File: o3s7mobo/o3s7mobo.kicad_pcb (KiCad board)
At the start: 2 copper layers, 330 x 217 mm, 45 parts, among them M1541 M1541, M1543 M1543

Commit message: Per feedback, swapped keyboard DIN
Replaced 5-pin with 7-pin, so that while standard AT keyboards (and adapters) will still work, users can make PS/2 mouse adapters without needing an ATX form card or a case with a PS/2 mouse port
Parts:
- moved KEYBOARD 0.81 mm to (18.0, 26.5)
- renumbered REF** to AGP, REF** to ATXpower, REF** to ATpower, REF** to PS2, REF** to SATA1_0, REF** to SATA1_1, REF** to SATA1_2, REF** to SATA1_3, REF** to SDRAM1, REF** to SDRAM2, REF** to SDRAM3, REF** to SiI3114CTU, REF** to VT6212L

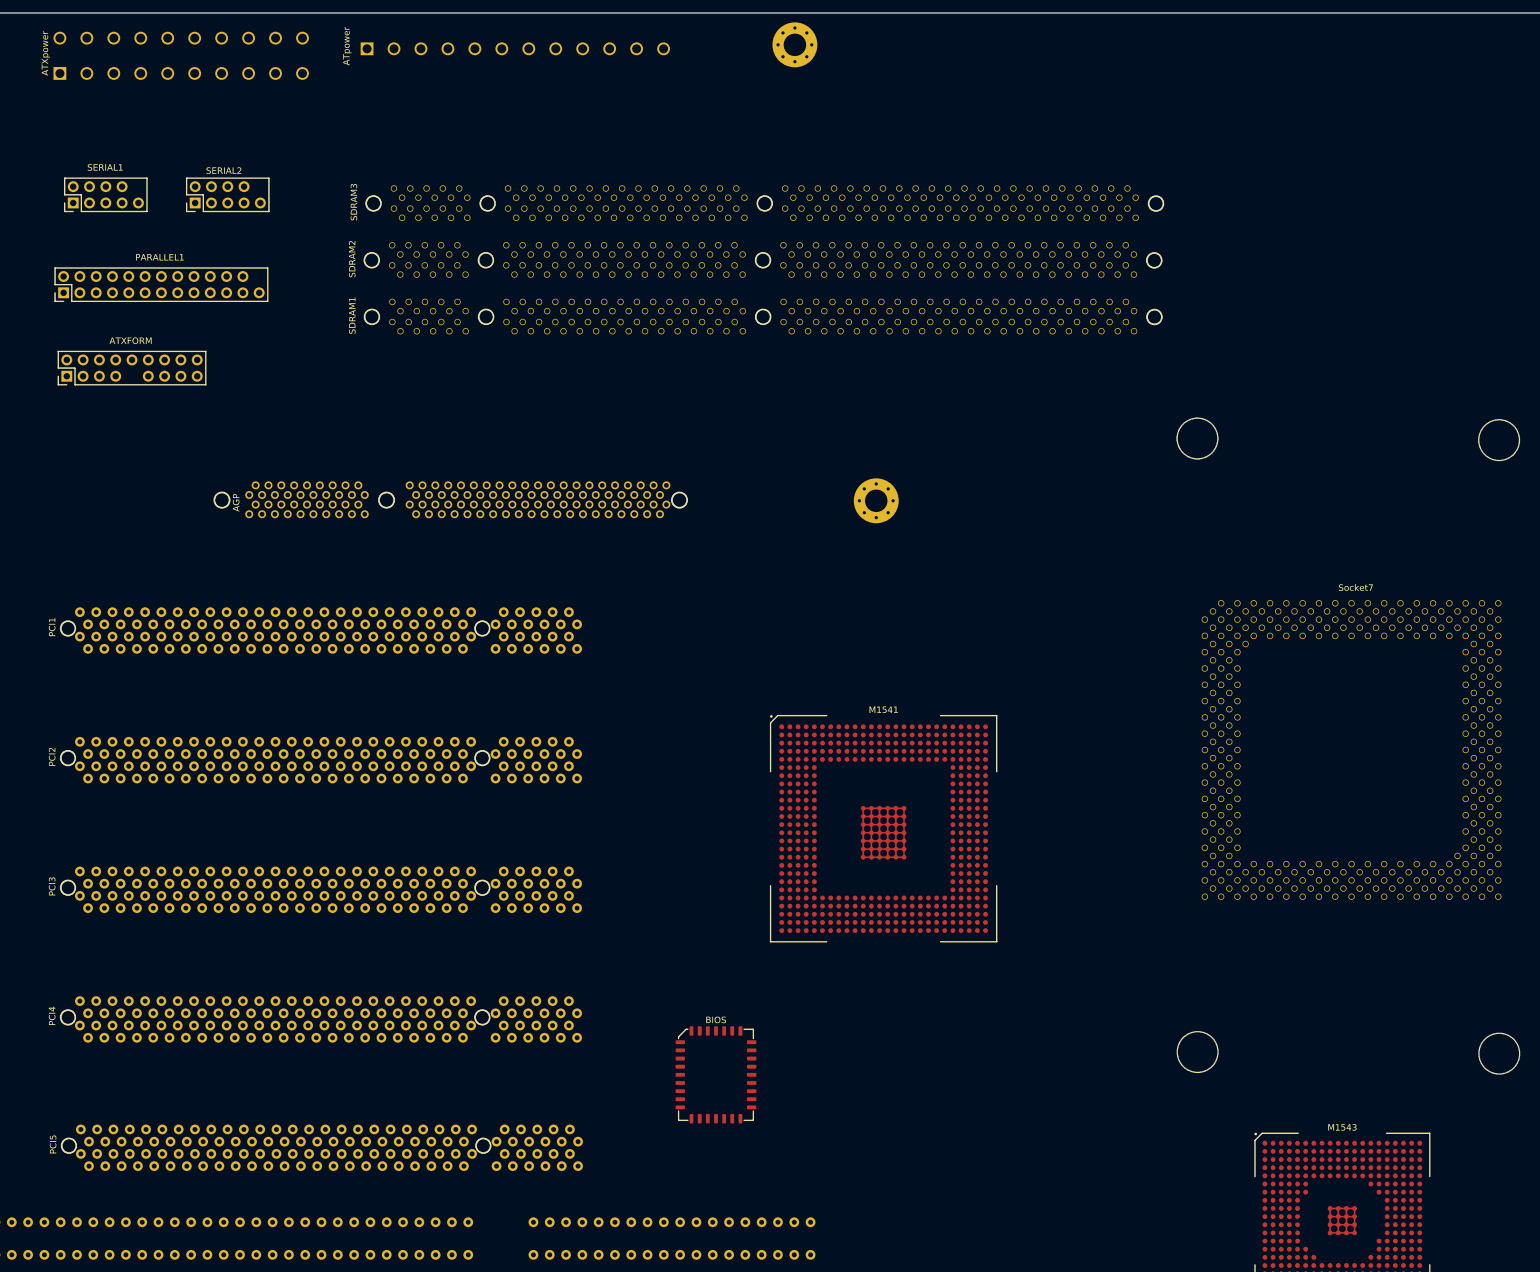
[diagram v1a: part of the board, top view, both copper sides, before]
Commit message: Added ATX and AT power schematics
This took way too long to figure out.
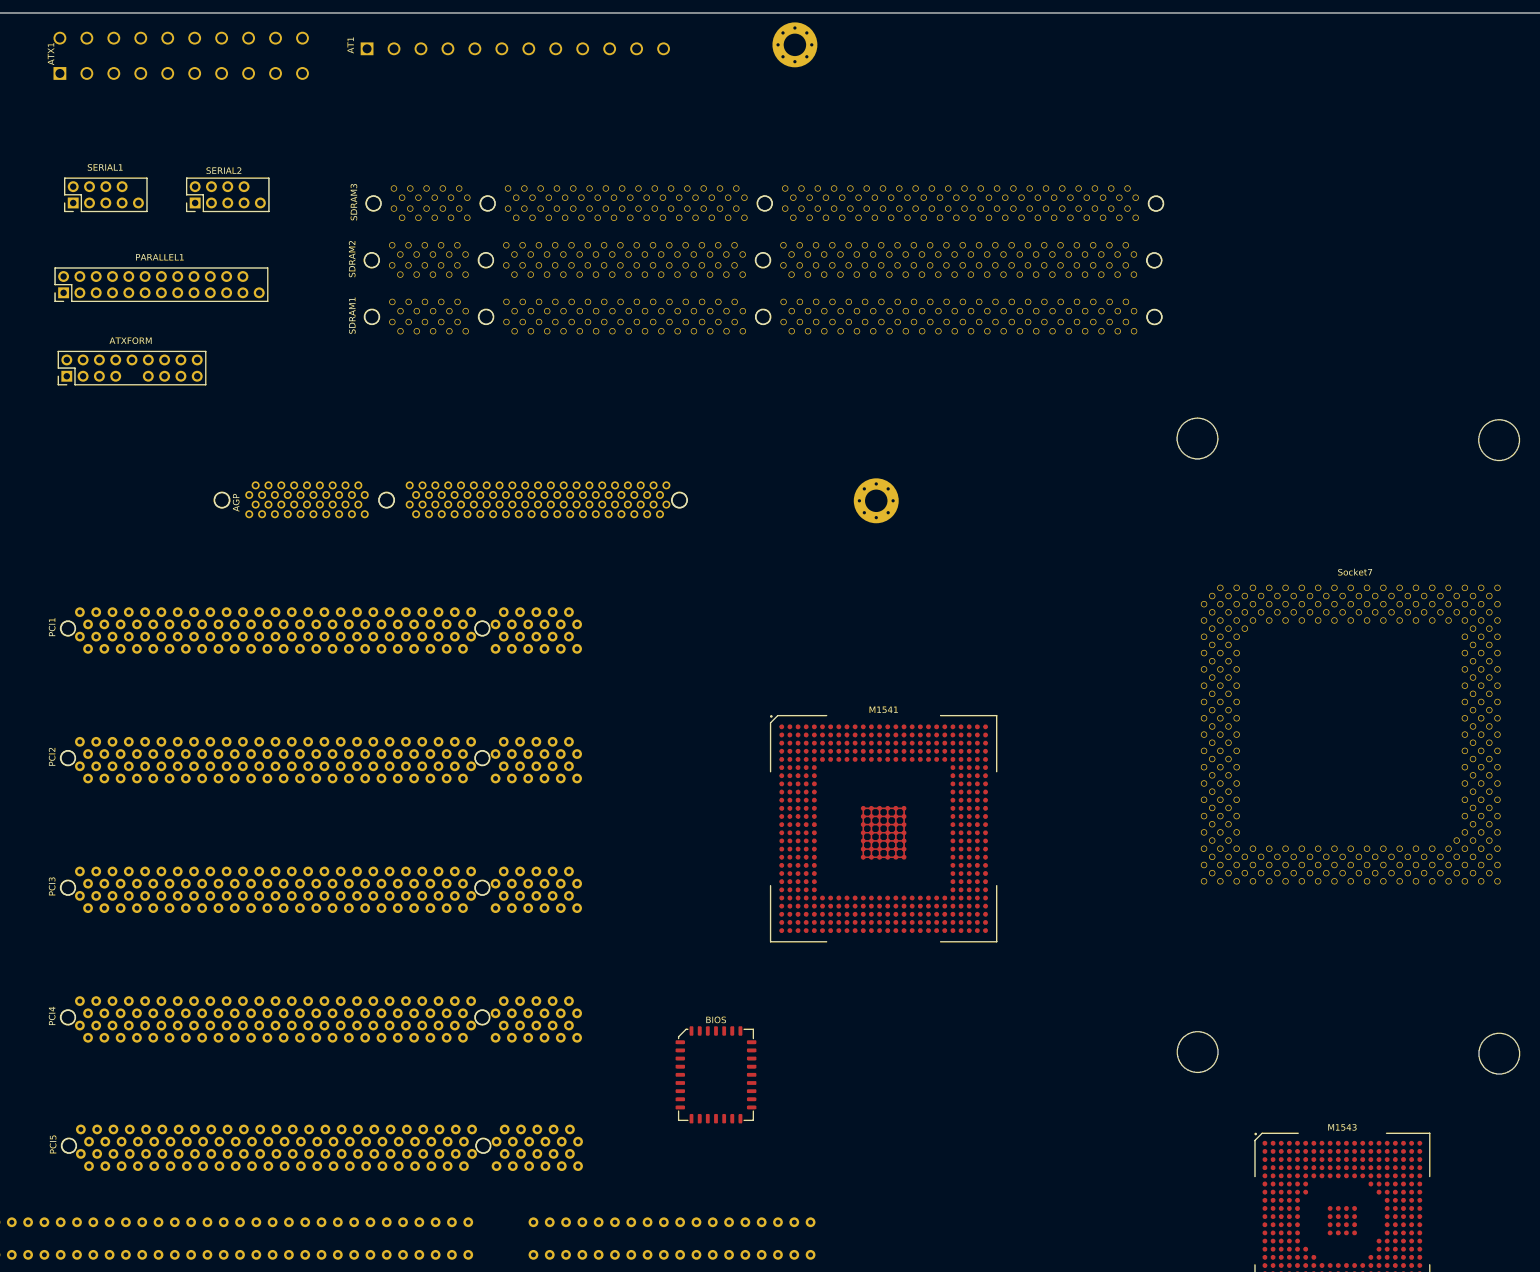
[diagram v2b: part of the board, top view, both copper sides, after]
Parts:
- removed ATXpower: ATXpower, Downloaded:ATXpower
- removed ATpower: ATpower, Downloaded:ATpower
- added AT1: AT-12, Downloaded:ATpower, F.Cu at (82.7, 4.00)
- added ATX1: ATX-20, Downloaded:ATXpower, F.Cu at (36.0, 5.35)
- moved Socket7 2.40 mm to (223.3, 86.8)
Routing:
- net (no net): track 120.6 -> 90.2 mm

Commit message: Added Socket 7 schematics
I'm willing to have these schematics uploaded to the official KiCAD repositories; I'm just unsure how.
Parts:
- removed Socket7: Socket_7, Downloaded:Socket_7
- added CPU1: Socket7, Downloaded:Socket_7, F.Cu at (223.3, 86.8)
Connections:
- net Net-(AT1-Pad1) renamed PWR_GOOD
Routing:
- net GND: track 0.00 -> 547.4 mm
- net Net-(CPU1-PadA19): track 0.00 -> 115.7 mm
- net Net-(CPU1-PadA11): track 0.00 -> 104.0 mm
- net PWR_+5V: track 0.00 -> 93.2 mm
- net PWR_-12V: track 0.00 -> 59.4 mm
- net PWR_-5V: track 0.00 -> 54.9 mm, vias 0 -> 1
- net PWR_+12V: track 0.00 -> 22.3 mm
- net PWR_+3.3V: track 0.00 -> 9.70 mm
- net Net-(CPU1-PadAN1): track 0.00 -> 2.54 mm
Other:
- copper layers 2 -> 4

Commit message: Been too long
Forgot I never pushed this.
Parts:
- removed M1541: M1541, Downloaded:M1541
- added NB1: M1542, Downloaded:M1541, F.Cu at (165.7, 117.3)
- PCI1, PCI2, PCI3, PCI4: value PCI -> Bus_PCI_32bit_5V
- moved CPU1 57.2 mm to (253.7, 135.3), turned to 180 degrees
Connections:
- CPU1 pad A31: /D22 -> CPU_D22
- CPU1 pad A33: /D18 -> CPU_D18
- CPU1 pad A35: /D15 -> CPU_D15
- CPU1 pad A5: /D41 -> CPU_D41
- CPU1 pad AE33: /A23 -> CPU_A23
- CPU1 pad AF34: /A21 -> CPU_A21
- CPU1 pad AG33: /A27 -> CPU_A27
- CPU1 pad AG35: /A24 -> CPU_A24
- CPU1 pad AH34: /A26 -> CPU_A26
- CPU1 pad AH36: /A22 -> CPU_A22
- CPU1 pad AJ33: /A31 -> CPU_A31
- CPU1 pad AJ35: /A25 -> CPU_A25
- CPU1 pad AK22: /A19 -> CPU_A19
- CPU1 pad AK24: /A17 -> CPU_A17
- CPU1 pad AK26: /A15 -> CPU_A15
- CPU1 pad AK28: /A13 -> CPU_A13
- CPU1 pad AK30: /A9 -> CPU_A9
- CPU1 pad AK32: /A5 -> CPU_A5
- CPU1 pad AK34: /A29 -> CPU_A29
- CPU1 pad AK36: /A28 -> CPU_A28
- CPU1 pad AL21: /A20 -> CPU_A20
- CPU1 pad AL23: /A18 -> CPU_A18
- CPU1 pad AL25: /A16 -> CPU_A16
- CPU1 pad AL27: /A14 -> CPU_A14
- CPU1 pad AL29: /A12 -> CPU_A12
- CPU1 pad AL31: /A11 -> CPU_A11
- CPU1 pad AL33: /A7 -> CPU_A7
- CPU1 pad AL35: /A3 -> CPU_A3
- CPU1 pad AM32: /A8 -> CPU_A8
- CPU1 pad AM34: /A4 -> CPU_A4
- CPU1 pad AM36: /A30 -> CPU_A30
- CPU1 pad AN31: /A10 -> CPU_A10
- CPU1 pad AN33: /A6 -> CPU_A6
- CPU1 pad B30: /D20 -> CPU_D20
- CPU1 pad B32: /D16 -> CPU_D16
- CPU1 pad B34: /D13 -> CPU_D13
- CPU1 pad B36: /D11 -> CPU_D11
- CPU1 pad B4: /D43 -> CPU_D43
- CPU1 pad C11: /D36 -> CPU_D36
- CPU1 pad C13: /D34 -> CPU_D34
- CPU1 pad C15: /D32 -> CPU_D32
- CPU1 pad C17: /D31 -> CPU_D31
- CPU1 pad C19: /D29 -> CPU_D29
- CPU1 pad C21: /D27 -> CPU_D27
- CPU1 pad C23: /D25 -> CPU_D25
- CPU1 pad C27: /D24 -> CPU_D24
- CPU1 pad C29: /D21 -> CPU_D21
- CPU1 pad C3: /D47 -> CPU_D47
- CPU1 pad C31: /D17 -> CPU_D17
- CPU1 pad C33: /D14 -> CPU_D14
- CPU1 pad C35: /D10 -> CPU_D10
- CPU1 pad C37: /D9 -> CPU_D9
- CPU1 pad C5: /D45 -> CPU_D45
- CPU1 pad C9: /D38 -> CPU_D38
- CPU1 pad D10: /D39 -> CPU_D39
- CPU1 pad D12: /D37 -> CPU_D37
- CPU1 pad D14: /D35 -> CPU_D35
- CPU1 pad D16: /D33 -> CPU_D33
- CPU1 pad D2: /D50 -> CPU_D50
- CPU1 pad D20: /D30 -> CPU_D30
- CPU1 pad D22: /D28 -> CPU_D28
- CPU1 pad D24: /D26 -> CPU_D26
- CPU1 pad D26: /D23 -> CPU_D23
- CPU1 pad D28: /D19 -> CPU_D19
- CPU1 pad D32: /D12 -> CPU_D12
- CPU1 pad D34: /D8 -> CPU_D8
- CPU1 pad D4: /D48 -> CPU_D48
- CPU1 pad D6: /D44 -> CPU_D44
- CPU1 pad D8: /D40 -> CPU_D40
- CPU1 pad E1: /D54 -> CPU_D54
- CPU1 pad E3: /D52 -> CPU_D52
- CPU1 pad E33: /D7 -> CPU_D7
- CPU1 pad E35: /D6 -> CPU_D6
- CPU1 pad E5: /D49 -> CPU_D49
- CPU1 pad E7: /D46 -> CPU_D46
- CPU1 pad E9: /D42 -> CPU_D42
- CPU1 pad F34: /D5 -> CPU_D5
- CPU1 pad F36: /D4 -> CPU_D4
- CPU1 pad F4: /D51 -> CPU_D51
- CPU1 pad G3: /D55 -> CPU_D55
- CPU1 pad G33: /D3 -> CPU_D3
- CPU1 pad G35: /D1 -> CPU_D1
- CPU1 pad G5: /D53 -> CPU_D53
- CPU1 pad H4: /D56 -> CPU_D56
- CPU1 pad J3: /D57 -> CPU_D57
- CPU1 pad J35: /D2 -> CPU_D2
- CPU1 pad J5: /D58 -> CPU_D58
- CPU1 pad K34: /D0 -> CPU_D0
- CPU1 pad K4: /D59 -> CPU_D59
- CPU1 pad L3: /D61 -> CPU_D61
- CPU1 pad L5: /D60 -> CPU_D60
- CPU1 pad M4: /D62 -> CPU_D62
- CPU1 pad N3: /D63 -> CPU_D63
- PCI1 pad A1: (no net) -> Net-(PCI1-PadA1)
- PCI1 pad A10: (no net) -> Net-(PCI1-PadA10)
- PCI1 pad A11: (no net) -> Net-(PCI1-PadA11)
- PCI1 pad A12: (no net) -> Net-(PCI1-PadA12)
- PCI1 pad A13: (no net) -> Net-(PCI1-PadA13)
- PCI1 pad A14: (no net) -> Net-(PCI1-PadA14)
- PCI1 pad A15: (no net) -> Net-(PCI1-PadA15)
- PCI1 pad A16: (no net) -> Net-(PCI1-PadA16)
- PCI1 pad A17: (no net) -> Net-(PCI1-PadA17)
- PCI1 pad A18: (no net) -> Net-(PCI1-PadA18)
- PCI1 pad A19: (no net) -> Net-(PCI1-PadA19)
- PCI1 pad A2: (no net) -> Net-(PCI1-PadA2)
- PCI1 pad A20: (no net) -> Net-(PCI1-PadA20)
- PCI1 pad A21: (no net) -> Net-(PCI1-PadA21)
- PCI1 pad A22: (no net) -> Net-(PCI1-PadA22)
- PCI1 pad A23: (no net) -> Net-(PCI1-PadA23)
- PCI1 pad A24: (no net) -> Net-(PCI1-PadA24)
- PCI1 pad A25: (no net) -> Net-(PCI1-PadA25)
- PCI1 pad A26: (no net) -> Net-(PCI1-PadA26)
- PCI1 pad A27: (no net) -> Net-(PCI1-PadA27)
- PCI1 pad A28: (no net) -> Net-(PCI1-PadA28)
- PCI1 pad A29: (no net) -> Net-(PCI1-PadA29)
- PCI1 pad A3: (no net) -> Net-(PCI1-PadA3)
- PCI1 pad A30: (no net) -> Net-(PCI1-PadA30)
- PCI1 pad A31: (no net) -> Net-(PCI1-PadA31)
- PCI1 pad A32: (no net) -> Net-(PCI1-PadA32)
- PCI1 pad A33: (no net) -> Net-(PCI1-PadA33)
- PCI1 pad A34: (no net) -> Net-(PCI1-PadA34)
- PCI1 pad A35: (no net) -> Net-(PCI1-PadA35)
- PCI1 pad A36: (no net) -> Net-(PCI1-PadA36)
- PCI1 pad A37: (no net) -> Net-(PCI1-PadA37)
- PCI1 pad A38: (no net) -> Net-(PCI1-PadA38)
- PCI1 pad A39: (no net) -> Net-(PCI1-PadA39)
- PCI1 pad A4: (no net) -> Net-(PCI1-PadA4)
- PCI1 pad A40: (no net) -> Net-(PCI1-PadA40)
- PCI1 pad A41: (no net) -> Net-(PCI1-PadA41)
- PCI1 pad A42: (no net) -> Net-(PCI1-PadA42)
- PCI1 pad A43: (no net) -> Net-(PCI1-PadA43)
- PCI1 pad A44: (no net) -> Net-(PCI1-PadA44)
- PCI1 pad A45: (no net) -> Net-(PCI1-PadA45)
- PCI1 pad A46: (no net) -> Net-(PCI1-PadA46)
- PCI1 pad A47: (no net) -> Net-(PCI1-PadA47)
- PCI1 pad A48: (no net) -> Net-(PCI1-PadA48)
- PCI1 pad A49: (no net) -> Net-(PCI1-PadA49)
- PCI1 pad A5: (no net) -> Net-(PCI1-PadA5)
- PCI1 pad A52: (no net) -> Net-(PCI1-PadA52)
- PCI1 pad A53: (no net) -> Net-(PCI1-PadA53)
- PCI1 pad A54: (no net) -> Net-(PCI1-PadA54)
- PCI1 pad A55: (no net) -> Net-(PCI1-PadA55)
- PCI1 pad A56: (no net) -> Net-(PCI1-PadA56)
- PCI1 pad A57: (no net) -> Net-(PCI1-PadA57)
- PCI1 pad A58: (no net) -> Net-(PCI1-PadA58)
- PCI1 pad A59: (no net) -> Net-(PCI1-PadA59)
- PCI1 pad A6: (no net) -> Net-(PCI1-PadA6)
- PCI1 pad A60: (no net) -> Net-(PCI1-PadA60)
- PCI1 pad A61: (no net) -> Net-(PCI1-PadA61)
- PCI1 pad A62: (no net) -> Net-(PCI1-PadA62)
- PCI1 pad A7: (no net) -> Net-(PCI1-PadA7)
- PCI1 pad A8: (no net) -> Net-(PCI1-PadA8)
- PCI1 pad A9: (no net) -> Net-(PCI1-PadA9)
- PCI1 pad B1: (no net) -> Net-(PCI1-PadB1)
- PCI1 pad B10: (no net) -> Net-(PCI1-PadB10)
- PCI1 pad B11: (no net) -> Net-(PCI1-PadB11)
- PCI1 pad B12: (no net) -> Net-(PCI1-PadB12)
- PCI1 pad B13: (no net) -> Net-(PCI1-PadB13)
- PCI1 pad B14: (no net) -> Net-(PCI1-PadB14)
- PCI1 pad B15: (no net) -> Net-(PCI1-PadB15)
- PCI1 pad B16: (no net) -> Net-(PCI1-PadB16)
- PCI1 pad B17: (no net) -> Net-(PCI1-PadB17)
- PCI1 pad B18: (no net) -> Net-(PCI1-PadB18)
- PCI1 pad B19: (no net) -> Net-(PCI1-PadB19)
- PCI1 pad B2: (no net) -> Net-(PCI1-PadB2)
- PCI1 pad B20: (no net) -> Net-(PCI1-PadB20)
- PCI1 pad B21: (no net) -> Net-(PCI1-PadB21)
- PCI1 pad B22: (no net) -> Net-(PCI1-PadB22)
- PCI1 pad B23: (no net) -> Net-(PCI1-PadB23)
- PCI1 pad B24: (no net) -> Net-(PCI1-PadB24)
- PCI1 pad B25: (no net) -> Net-(PCI1-PadB25)
- PCI1 pad B26: (no net) -> Net-(PCI1-PadB26)
- PCI1 pad B27: (no net) -> Net-(PCI1-PadB27)
- PCI1 pad B28: (no net) -> Net-(PCI1-PadB28)
- PCI1 pad B29: (no net) -> Net-(PCI1-PadB29)
- PCI1 pad B3: (no net) -> Net-(PCI1-PadB3)
- PCI1 pad B30: (no net) -> Net-(PCI1-PadB30)
- PCI1 pad B31: (no net) -> Net-(PCI1-PadB31)
- PCI1 pad B32: (no net) -> Net-(PCI1-PadB32)
- PCI1 pad B33: (no net) -> Net-(PCI1-PadB33)
- PCI1 pad B34: (no net) -> Net-(PCI1-PadB34)
- PCI1 pad B35: (no net) -> Net-(PCI1-PadB35)
- PCI1 pad B36: (no net) -> Net-(PCI1-PadB36)
- PCI1 pad B37: (no net) -> Net-(PCI1-PadB37)
- PCI1 pad B38: (no net) -> Net-(PCI1-PadB38)
- PCI1 pad B39: (no net) -> Net-(PCI1-PadB39)
- PCI1 pad B4: (no net) -> Net-(PCI1-PadB4)
- PCI1 pad B40: (no net) -> Net-(PCI1-PadB40)
- PCI1 pad B41: (no net) -> Net-(PCI1-PadB41)
- PCI1 pad B42: (no net) -> Net-(PCI1-PadB42)
- PCI1 pad B43: (no net) -> Net-(PCI1-PadB43)
- PCI1 pad B44: (no net) -> Net-(PCI1-PadB44)
- PCI1 pad B45: (no net) -> Net-(PCI1-PadB45)
- PCI1 pad B46: (no net) -> Net-(PCI1-PadB46)
- PCI1 pad B47: (no net) -> Net-(PCI1-PadB47)
- PCI1 pad B48: (no net) -> Net-(PCI1-PadB48)
- PCI1 pad B49: (no net) -> Net-(PCI1-PadB49)
- PCI1 pad B5: (no net) -> Net-(PCI1-PadB5)
- PCI1 pad B52: (no net) -> Net-(PCI1-PadB52)
- PCI1 pad B53: (no net) -> Net-(PCI1-PadB53)
- PCI1 pad B54: (no net) -> Net-(PCI1-PadB54)
- PCI1 pad B55: (no net) -> Net-(PCI1-PadB55)
- PCI1 pad B56: (no net) -> Net-(PCI1-PadB56)
- PCI1 pad B57: (no net) -> Net-(PCI1-PadB57)
- PCI1 pad B58: (no net) -> Net-(PCI1-PadB58)
- PCI1 pad B59: (no net) -> Net-(PCI1-PadB59)
- PCI1 pad B6: (no net) -> Net-(PCI1-PadB6)
- PCI1 pad B60: (no net) -> Net-(PCI1-PadB60)
- PCI1 pad B61: (no net) -> Net-(PCI1-PadB61)
- PCI1 pad B62: (no net) -> Net-(PCI1-PadB62)
- PCI1 pad B7: (no net) -> Net-(PCI1-PadB7)
- PCI1 pad B8: (no net) -> Net-(PCI1-PadB8)
- PCI1 pad B9: (no net) -> Net-(PCI1-PadB9)
- PCI2 pad A1: (no net) -> Net-(PCI2-PadA1)
- PCI2 pad A10: (no net) -> Net-(PCI2-PadA10)
- PCI2 pad A11: (no net) -> Net-(PCI2-PadA11)
- PCI2 pad A12: (no net) -> Net-(PCI2-PadA12)
- PCI2 pad A13: (no net) -> Net-(PCI2-PadA13)
- PCI2 pad A14: (no net) -> Net-(PCI2-PadA14)
- PCI2 pad A15: (no net) -> Net-(PCI2-PadA15)
- PCI2 pad A16: (no net) -> Net-(PCI2-PadA16)
- PCI2 pad A17: (no net) -> Net-(PCI2-PadA17)
- PCI2 pad A18: (no net) -> Net-(PCI2-PadA18)
- PCI2 pad A19: (no net) -> Net-(PCI2-PadA19)
- PCI2 pad A2: (no net) -> Net-(PCI2-PadA2)
- PCI2 pad A20: (no net) -> Net-(PCI2-PadA20)
- PCI2 pad A21: (no net) -> Net-(PCI2-PadA21)
- PCI2 pad A22: (no net) -> Net-(PCI2-PadA22)
- PCI2 pad A23: (no net) -> Net-(PCI2-PadA23)
- PCI2 pad A24: (no net) -> Net-(PCI2-PadA24)
- PCI2 pad A25: (no net) -> Net-(PCI2-PadA25)
- PCI2 pad A26: (no net) -> Net-(PCI2-PadA26)
- PCI2 pad A27: (no net) -> Net-(PCI2-PadA27)
- PCI2 pad A28: (no net) -> Net-(PCI2-PadA28)
- PCI2 pad A29: (no net) -> Net-(PCI2-PadA29)
- PCI2 pad A3: (no net) -> Net-(PCI2-PadA3)
- PCI2 pad A30: (no net) -> Net-(PCI2-PadA30)
- PCI2 pad A31: (no net) -> Net-(PCI2-PadA31)
- PCI2 pad A32: (no net) -> Net-(PCI2-PadA32)
- PCI2 pad A33: (no net) -> Net-(PCI2-PadA33)
- PCI2 pad A34: (no net) -> Net-(PCI2-PadA34)
- PCI2 pad A35: (no net) -> Net-(PCI2-PadA35)
- PCI2 pad A36: (no net) -> Net-(PCI2-PadA36)
- PCI2 pad A37: (no net) -> Net-(PCI2-PadA37)
- PCI2 pad A38: (no net) -> Net-(PCI2-PadA38)
- PCI2 pad A39: (no net) -> Net-(PCI2-PadA39)
- PCI2 pad A4: (no net) -> Net-(PCI2-PadA4)
- PCI2 pad A40: (no net) -> Net-(PCI2-PadA40)
- PCI2 pad A41: (no net) -> Net-(PCI2-PadA41)
- PCI2 pad A42: (no net) -> Net-(PCI2-PadA42)
- PCI2 pad A43: (no net) -> Net-(PCI2-PadA43)
- PCI2 pad A44: (no net) -> Net-(PCI2-PadA44)
- PCI2 pad A45: (no net) -> Net-(PCI2-PadA45)
- PCI2 pad A46: (no net) -> Net-(PCI2-PadA46)
- PCI2 pad A47: (no net) -> Net-(PCI2-PadA47)
- PCI2 pad A48: (no net) -> Net-(PCI2-PadA48)
- PCI2 pad A49: (no net) -> Net-(PCI2-PadA49)
- PCI2 pad A5: (no net) -> Net-(PCI2-PadA5)
- PCI2 pad A52: (no net) -> Net-(PCI2-PadA52)
- PCI2 pad A53: (no net) -> Net-(PCI2-PadA53)
- PCI2 pad A54: (no net) -> Net-(PCI2-PadA54)
- PCI2 pad A55: (no net) -> Net-(PCI2-PadA55)
- PCI2 pad A56: (no net) -> Net-(PCI2-PadA56)
- PCI2 pad A57: (no net) -> Net-(PCI2-PadA57)
- PCI2 pad A58: (no net) -> Net-(PCI2-PadA58)
- PCI2 pad A59: (no net) -> Net-(PCI2-PadA59)
- PCI2 pad A6: (no net) -> Net-(PCI2-PadA6)
- PCI2 pad A60: (no net) -> Net-(PCI2-PadA60)
- PCI2 pad A61: (no net) -> Net-(PCI2-PadA61)
- PCI2 pad A62: (no net) -> Net-(PCI2-PadA62)
- PCI2 pad A7: (no net) -> Net-(PCI2-PadA7)
- PCI2 pad A8: (no net) -> Net-(PCI2-PadA8)
- PCI2 pad A9: (no net) -> Net-(PCI2-PadA9)
- PCI2 pad B1: (no net) -> Net-(PCI2-PadB1)
- PCI2 pad B10: (no net) -> Net-(PCI2-PadB10)
- PCI2 pad B11: (no net) -> Net-(PCI2-PadB11)
- PCI2 pad B12: (no net) -> Net-(PCI2-PadB12)
- PCI2 pad B13: (no net) -> Net-(PCI2-PadB13)
- PCI2 pad B14: (no net) -> Net-(PCI2-PadB14)
- PCI2 pad B15: (no net) -> Net-(PCI2-PadB15)
- PCI2 pad B16: (no net) -> Net-(PCI2-PadB16)
- PCI2 pad B17: (no net) -> Net-(PCI2-PadB17)
- PCI2 pad B18: (no net) -> Net-(PCI2-PadB18)
- PCI2 pad B19: (no net) -> Net-(PCI2-PadB19)
- PCI2 pad B2: (no net) -> Net-(PCI2-PadB2)
- PCI2 pad B20: (no net) -> Net-(PCI2-PadB20)
- PCI2 pad B21: (no net) -> Net-(PCI2-PadB21)
- PCI2 pad B22: (no net) -> Net-(PCI2-PadB22)
- PCI2 pad B23: (no net) -> Net-(PCI2-PadB23)
- PCI2 pad B24: (no net) -> Net-(PCI2-PadB24)
- PCI2 pad B25: (no net) -> Net-(PCI2-PadB25)
- PCI2 pad B26: (no net) -> Net-(PCI2-PadB26)
- PCI2 pad B27: (no net) -> Net-(PCI2-PadB27)
- PCI2 pad B28: (no net) -> Net-(PCI2-PadB28)
- PCI2 pad B29: (no net) -> Net-(PCI2-PadB29)
- PCI2 pad B3: (no net) -> Net-(PCI2-PadB3)
- PCI2 pad B30: (no net) -> Net-(PCI2-PadB30)
- PCI2 pad B31: (no net) -> Net-(PCI2-PadB31)
- PCI2 pad B32: (no net) -> Net-(PCI2-PadB32)
- PCI2 pad B33: (no net) -> Net-(PCI2-PadB33)
- PCI2 pad B34: (no net) -> Net-(PCI2-PadB34)
- PCI2 pad B35: (no net) -> Net-(PCI2-PadB35)
- PCI2 pad B36: (no net) -> Net-(PCI2-PadB36)
- PCI2 pad B37: (no net) -> Net-(PCI2-PadB37)
- PCI2 pad B38: (no net) -> Net-(PCI2-PadB38)
- PCI2 pad B39: (no net) -> Net-(PCI2-PadB39)
- PCI2 pad B4: (no net) -> Net-(PCI2-PadB4)
- PCI2 pad B40: (no net) -> Net-(PCI2-PadB40)
- PCI2 pad B41: (no net) -> Net-(PCI2-PadB41)
- PCI2 pad B42: (no net) -> Net-(PCI2-PadB42)
- PCI2 pad B43: (no net) -> Net-(PCI2-PadB43)
- PCI2 pad B44: (no net) -> Net-(PCI2-PadB44)
- PCI2 pad B45: (no net) -> Net-(PCI2-PadB45)
- PCI2 pad B46: (no net) -> Net-(PCI2-PadB46)
- PCI2 pad B47: (no net) -> Net-(PCI2-PadB47)
- PCI2 pad B48: (no net) -> Net-(PCI2-PadB48)
- PCI2 pad B49: (no net) -> Net-(PCI2-PadB49)
- PCI2 pad B5: (no net) -> Net-(PCI2-PadB5)
- PCI2 pad B52: (no net) -> Net-(PCI2-PadB52)
- PCI2 pad B53: (no net) -> Net-(PCI2-PadB53)
- PCI2 pad B54: (no net) -> Net-(PCI2-PadB54)
- PCI2 pad B55: (no net) -> Net-(PCI2-PadB55)
- PCI2 pad B56: (no net) -> Net-(PCI2-PadB56)
- PCI2 pad B57: (no net) -> Net-(PCI2-PadB57)
- PCI2 pad B58: (no net) -> Net-(PCI2-PadB58)
- PCI2 pad B59: (no net) -> Net-(PCI2-PadB59)
- PCI2 pad B6: (no net) -> Net-(PCI2-PadB6)
- PCI2 pad B60: (no net) -> Net-(PCI2-PadB60)
- PCI2 pad B61: (no net) -> Net-(PCI2-PadB61)
- PCI2 pad B62: (no net) -> Net-(PCI2-PadB62)
- PCI2 pad B7: (no net) -> Net-(PCI2-PadB7)
- PCI2 pad B8: (no net) -> Net-(PCI2-PadB8)
- PCI2 pad B9: (no net) -> Net-(PCI2-PadB9)
- PCI3 pad A1: (no net) -> Net-(PCI3-PadA1)
- PCI3 pad A10: (no net) -> Net-(PCI3-PadA10)
- PCI3 pad A11: (no net) -> Net-(PCI3-PadA11)
- PCI3 pad A12: (no net) -> Net-(PCI3-PadA12)
- PCI3 pad A13: (no net) -> Net-(PCI3-PadA13)
- PCI3 pad A14: (no net) -> Net-(PCI3-PadA14)
- PCI3 pad A15: (no net) -> Net-(PCI3-PadA15)
- PCI3 pad A16: (no net) -> Net-(PCI3-PadA16)
- PCI3 pad A17: (no net) -> Net-(PCI3-PadA17)
- PCI3 pad A18: (no net) -> Net-(PCI3-PadA18)
- PCI3 pad A19: (no net) -> Net-(PCI3-PadA19)
- PCI3 pad A2: (no net) -> Net-(PCI3-PadA2)
- PCI3 pad A20: (no net) -> Net-(PCI3-PadA20)
- PCI3 pad A21: (no net) -> Net-(PCI3-PadA21)
- PCI3 pad A22: (no net) -> Net-(PCI3-PadA22)
- PCI3 pad A23: (no net) -> Net-(PCI3-PadA23)
- PCI3 pad A24: (no net) -> Net-(PCI3-PadA24)
- PCI3 pad A25: (no net) -> Net-(PCI3-PadA25)
- PCI3 pad A26: (no net) -> Net-(PCI3-PadA26)
- PCI3 pad A27: (no net) -> Net-(PCI3-PadA27)
- PCI3 pad A28: (no net) -> Net-(PCI3-PadA28)
- PCI3 pad A29: (no net) -> Net-(PCI3-PadA29)
- PCI3 pad A3: (no net) -> Net-(PCI3-PadA3)
- PCI3 pad A30: (no net) -> Net-(PCI3-PadA30)
- PCI3 pad A31: (no net) -> Net-(PCI3-PadA31)
- PCI3 pad A32: (no net) -> Net-(PCI3-PadA32)
- PCI3 pad A33: (no net) -> Net-(PCI3-PadA33)
- PCI3 pad A34: (no net) -> Net-(PCI3-PadA34)
- PCI3 pad A35: (no net) -> Net-(PCI3-PadA35)
- PCI3 pad A36: (no net) -> Net-(PCI3-PadA36)
- PCI3 pad A37: (no net) -> Net-(PCI3-PadA37)
- PCI3 pad A38: (no net) -> Net-(PCI3-PadA38)
- PCI3 pad A39: (no net) -> Net-(PCI3-PadA39)
- PCI3 pad A4: (no net) -> Net-(PCI3-PadA4)
- PCI3 pad A40: (no net) -> Net-(PCI3-PadA40)
- PCI3 pad A41: (no net) -> Net-(PCI3-PadA41)
- PCI3 pad A42: (no net) -> Net-(PCI3-PadA42)
- PCI3 pad A43: (no net) -> Net-(PCI3-PadA43)
- PCI3 pad A44: (no net) -> Net-(PCI3-PadA44)
- PCI3 pad A45: (no net) -> Net-(PCI3-PadA45)
- PCI3 pad A46: (no net) -> Net-(PCI3-PadA46)
- PCI3 pad A47: (no net) -> Net-(PCI3-PadA47)
- PCI3 pad A48: (no net) -> Net-(PCI3-PadA48)
- PCI3 pad A49: (no net) -> Net-(PCI3-PadA49)
- PCI3 pad A5: (no net) -> Net-(PCI3-PadA5)
- PCI3 pad A52: (no net) -> Net-(PCI3-PadA52)
- PCI3 pad A53: (no net) -> Net-(PCI3-PadA53)
- PCI3 pad A54: (no net) -> Net-(PCI3-PadA54)
- PCI3 pad A55: (no net) -> Net-(PCI3-PadA55)
- PCI3 pad A56: (no net) -> Net-(PCI3-PadA56)
- PCI3 pad A57: (no net) -> Net-(PCI3-PadA57)
- PCI3 pad A58: (no net) -> Net-(PCI3-PadA58)
- PCI3 pad A59: (no net) -> Net-(PCI3-PadA59)
- PCI3 pad A6: (no net) -> Net-(PCI3-PadA6)
- PCI3 pad A60: (no net) -> Net-(PCI3-PadA60)
- PCI3 pad A61: (no net) -> Net-(PCI3-PadA61)
- PCI3 pad A62: (no net) -> Net-(PCI3-PadA62)
- PCI3 pad A7: (no net) -> Net-(PCI3-PadA7)
- PCI3 pad A8: (no net) -> Net-(PCI3-PadA8)
- PCI3 pad A9: (no net) -> Net-(PCI3-PadA9)
- PCI3 pad B1: (no net) -> Net-(PCI3-PadB1)
- PCI3 pad B10: (no net) -> Net-(PCI3-PadB10)
- PCI3 pad B11: (no net) -> Net-(PCI3-PadB11)
- PCI3 pad B12: (no net) -> Net-(PCI3-PadB12)
- PCI3 pad B13: (no net) -> Net-(PCI3-PadB13)
- PCI3 pad B14: (no net) -> Net-(PCI3-PadB14)
- PCI3 pad B15: (no net) -> Net-(PCI3-PadB15)
- PCI3 pad B16: (no net) -> Net-(PCI3-PadB16)
- PCI3 pad B17: (no net) -> Net-(PCI3-PadB17)
- PCI3 pad B18: (no net) -> Net-(PCI3-PadB18)
- PCI3 pad B19: (no net) -> Net-(PCI3-PadB19)
- PCI3 pad B2: (no net) -> Net-(PCI3-PadB2)
- PCI3 pad B20: (no net) -> Net-(PCI3-PadB20)
- PCI3 pad B21: (no net) -> Net-(PCI3-PadB21)
- PCI3 pad B22: (no net) -> Net-(PCI3-PadB22)
- PCI3 pad B23: (no net) -> Net-(PCI3-PadB23)
- PCI3 pad B24: (no net) -> Net-(PCI3-PadB24)
- PCI3 pad B25: (no net) -> Net-(PCI3-PadB25)
- PCI3 pad B26: (no net) -> Net-(PCI3-PadB26)
- PCI3 pad B27: (no net) -> Net-(PCI3-PadB27)
- PCI3 pad B28: (no net) -> Net-(PCI3-PadB28)
- PCI3 pad B29: (no net) -> Net-(PCI3-PadB29)
- PCI3 pad B3: (no net) -> Net-(PCI3-PadB3)
- PCI3 pad B30: (no net) -> Net-(PCI3-PadB30)
- PCI3 pad B31: (no net) -> Net-(PCI3-PadB31)
- PCI3 pad B32: (no net) -> Net-(PCI3-PadB32)
- PCI3 pad B33: (no net) -> Net-(PCI3-PadB33)
- PCI3 pad B34: (no net) -> Net-(PCI3-PadB34)
- PCI3 pad B35: (no net) -> Net-(PCI3-PadB35)
- PCI3 pad B36: (no net) -> Net-(PCI3-PadB36)
- PCI3 pad B37: (no net) -> Net-(PCI3-PadB37)
- PCI3 pad B38: (no net) -> Net-(PCI3-PadB38)
- PCI3 pad B39: (no net) -> Net-(PCI3-PadB39)
- PCI3 pad B4: (no net) -> Net-(PCI3-PadB4)
- PCI3 pad B40: (no net) -> Net-(PCI3-PadB40)
- PCI3 pad B41: (no net) -> Net-(PCI3-PadB41)
- PCI3 pad B42: (no net) -> Net-(PCI3-PadB42)
- PCI3 pad B43: (no net) -> Net-(PCI3-PadB43)
- PCI3 pad B44: (no net) -> Net-(PCI3-PadB44)
- PCI3 pad B45: (no net) -> Net-(PCI3-PadB45)
- PCI3 pad B46: (no net) -> Net-(PCI3-PadB46)
- PCI3 pad B47: (no net) -> Net-(PCI3-PadB47)
- PCI3 pad B48: (no net) -> Net-(PCI3-PadB48)
- PCI3 pad B49: (no net) -> Net-(PCI3-PadB49)
- PCI3 pad B5: (no net) -> Net-(PCI3-PadB5)
- PCI3 pad B52: (no net) -> Net-(PCI3-PadB52)
- PCI3 pad B53: (no net) -> Net-(PCI3-PadB53)
- PCI3 pad B54: (no net) -> Net-(PCI3-PadB54)
- PCI3 pad B55: (no net) -> Net-(PCI3-PadB55)
- PCI3 pad B56: (no net) -> Net-(PCI3-PadB56)
- PCI3 pad B57: (no net) -> Net-(PCI3-PadB57)
- PCI3 pad B58: (no net) -> Net-(PCI3-PadB58)
- PCI3 pad B59: (no net) -> Net-(PCI3-PadB59)
- PCI3 pad B6: (no net) -> Net-(PCI3-PadB6)
- PCI3 pad B60: (no net) -> Net-(PCI3-PadB60)
- PCI3 pad B61: (no net) -> Net-(PCI3-PadB61)
- PCI3 pad B62: (no net) -> Net-(PCI3-PadB62)
- PCI3 pad B7: (no net) -> Net-(PCI3-PadB7)
- PCI3 pad B8: (no net) -> Net-(PCI3-PadB8)
- PCI3 pad B9: (no net) -> Net-(PCI3-PadB9)
- PCI4 pad A1: (no net) -> Net-(PCI4-PadA1)
- PCI4 pad A10: (no net) -> Net-(PCI4-PadA10)
- PCI4 pad A11: (no net) -> Net-(PCI4-PadA11)
- PCI4 pad A12: (no net) -> Net-(PCI4-PadA12)
- PCI4 pad A13: (no net) -> Net-(PCI4-PadA13)
- PCI4 pad A14: (no net) -> Net-(PCI4-PadA14)
- PCI4 pad A15: (no net) -> Net-(PCI4-PadA15)
- PCI4 pad A16: (no net) -> Net-(PCI4-PadA16)
- PCI4 pad A17: (no net) -> Net-(PCI4-PadA17)
- PCI4 pad A18: (no net) -> Net-(PCI4-PadA18)
- PCI4 pad A19: (no net) -> Net-(PCI4-PadA19)
- PCI4 pad A2: (no net) -> Net-(PCI4-PadA2)
- PCI4 pad A20: (no net) -> Net-(PCI4-PadA20)
- PCI4 pad A21: (no net) -> Net-(PCI4-PadA21)
- PCI4 pad A22: (no net) -> Net-(PCI4-PadA22)
- PCI4 pad A23: (no net) -> Net-(PCI4-PadA23)
- PCI4 pad A24: (no net) -> Net-(PCI4-PadA24)
- PCI4 pad A25: (no net) -> Net-(PCI4-PadA25)
- PCI4 pad A26: (no net) -> Net-(PCI4-PadA26)
- PCI4 pad A27: (no net) -> Net-(PCI4-PadA27)
- PCI4 pad A28: (no net) -> Net-(PCI4-PadA28)
- PCI4 pad A29: (no net) -> Net-(PCI4-PadA29)
- PCI4 pad A3: (no net) -> Net-(PCI4-PadA3)
- PCI4 pad A30: (no net) -> Net-(PCI4-PadA30)
- PCI4 pad A31: (no net) -> Net-(PCI4-PadA31)
- PCI4 pad A32: (no net) -> Net-(PCI4-PadA32)
- PCI4 pad A33: (no net) -> Net-(PCI4-PadA33)
- PCI4 pad A34: (no net) -> Net-(PCI4-PadA34)
- PCI4 pad A35: (no net) -> Net-(PCI4-PadA35)
- PCI4 pad A36: (no net) -> Net-(PCI4-PadA36)
- PCI4 pad A37: (no net) -> Net-(PCI4-PadA37)
- PCI4 pad A38: (no net) -> Net-(PCI4-PadA38)
- PCI4 pad A39: (no net) -> Net-(PCI4-PadA39)
- PCI4 pad A4: (no net) -> Net-(PCI4-PadA4)
- PCI4 pad A40: (no net) -> Net-(PCI4-PadA40)
- PCI4 pad A41: (no net) -> Net-(PCI4-PadA41)
- PCI4 pad A42: (no net) -> Net-(PCI4-PadA42)
- PCI4 pad A43: (no net) -> Net-(PCI4-PadA43)
- PCI4 pad A44: (no net) -> Net-(PCI4-PadA44)
- PCI4 pad A45: (no net) -> Net-(PCI4-PadA45)
- PCI4 pad A46: (no net) -> Net-(PCI4-PadA46)
- PCI4 pad A47: (no net) -> Net-(PCI4-PadA47)
- PCI4 pad A48: (no net) -> Net-(PCI4-PadA48)
- PCI4 pad A49: (no net) -> Net-(PCI4-PadA49)
- PCI4 pad A5: (no net) -> Net-(PCI4-PadA5)
- PCI4 pad A52: (no net) -> Net-(PCI4-PadA52)
- PCI4 pad A53: (no net) -> Net-(PCI4-PadA53)
- PCI4 pad A54: (no net) -> Net-(PCI4-PadA54)
- PCI4 pad A55: (no net) -> Net-(PCI4-PadA55)
- PCI4 pad A56: (no net) -> Net-(PCI4-PadA56)
- PCI4 pad A57: (no net) -> Net-(PCI4-PadA57)
- PCI4 pad A58: (no net) -> Net-(PCI4-PadA58)
- PCI4 pad A59: (no net) -> Net-(PCI4-PadA59)
- PCI4 pad A6: (no net) -> Net-(PCI4-PadA6)
- PCI4 pad A60: (no net) -> Net-(PCI4-PadA60)
- PCI4 pad A61: (no net) -> Net-(PCI4-PadA61)
- PCI4 pad A62: (no net) -> Net-(PCI4-PadA62)
- PCI4 pad A7: (no net) -> Net-(PCI4-PadA7)
- PCI4 pad A8: (no net) -> Net-(PCI4-PadA8)
- PCI4 pad A9: (no net) -> Net-(PCI4-PadA9)
- PCI4 pad B1: (no net) -> Net-(PCI4-PadB1)
- PCI4 pad B10: (no net) -> Net-(PCI4-PadB10)
- PCI4 pad B11: (no net) -> Net-(PCI4-PadB11)
- PCI4 pad B12: (no net) -> Net-(PCI4-PadB12)
- PCI4 pad B13: (no net) -> Net-(PCI4-PadB13)
- PCI4 pad B14: (no net) -> Net-(PCI4-PadB14)
- PCI4 pad B15: (no net) -> Net-(PCI4-PadB15)
- PCI4 pad B16: (no net) -> Net-(PCI4-PadB16)
- PCI4 pad B17: (no net) -> Net-(PCI4-PadB17)
- PCI4 pad B18: (no net) -> Net-(PCI4-PadB18)
- PCI4 pad B19: (no net) -> Net-(PCI4-PadB19)
- PCI4 pad B2: (no net) -> Net-(PCI4-PadB2)
- PCI4 pad B20: (no net) -> Net-(PCI4-PadB20)
- PCI4 pad B21: (no net) -> Net-(PCI4-PadB21)
- PCI4 pad B22: (no net) -> Net-(PCI4-PadB22)
- PCI4 pad B23: (no net) -> Net-(PCI4-PadB23)
- PCI4 pad B24: (no net) -> Net-(PCI4-PadB24)
- PCI4 pad B25: (no net) -> Net-(PCI4-PadB25)
- PCI4 pad B26: (no net) -> Net-(PCI4-PadB26)
- PCI4 pad B27: (no net) -> Net-(PCI4-PadB27)
- PCI4 pad B28: (no net) -> Net-(PCI4-PadB28)
- PCI4 pad B29: (no net) -> Net-(PCI4-PadB29)
- PCI4 pad B3: (no net) -> Net-(PCI4-PadB3)
- PCI4 pad B30: (no net) -> Net-(PCI4-PadB30)
- PCI4 pad B31: (no net) -> Net-(PCI4-PadB31)
- PCI4 pad B32: (no net) -> Net-(PCI4-PadB32)
- PCI4 pad B33: (no net) -> Net-(PCI4-PadB33)
- PCI4 pad B34: (no net) -> Net-(PCI4-PadB34)
- PCI4 pad B35: (no net) -> Net-(PCI4-PadB35)
- PCI4 pad B36: (no net) -> Net-(PCI4-PadB36)
- PCI4 pad B37: (no net) -> Net-(PCI4-PadB37)
- PCI4 pad B38: (no net) -> Net-(PCI4-PadB38)
- PCI4 pad B39: (no net) -> Net-(PCI4-PadB39)
- PCI4 pad B4: (no net) -> Net-(PCI4-PadB4)
- PCI4 pad B40: (no net) -> Net-(PCI4-PadB40)
- PCI4 pad B41: (no net) -> Net-(PCI4-PadB41)
- PCI4 pad B42: (no net) -> Net-(PCI4-PadB42)
- PCI4 pad B43: (no net) -> Net-(PCI4-PadB43)
- PCI4 pad B44: (no net) -> Net-(PCI4-PadB44)
- PCI4 pad B45: (no net) -> Net-(PCI4-PadB45)
- PCI4 pad B46: (no net) -> Net-(PCI4-PadB46)
- PCI4 pad B47: (no net) -> Net-(PCI4-PadB47)
- PCI4 pad B48: (no net) -> Net-(PCI4-PadB48)
- PCI4 pad B49: (no net) -> Net-(PCI4-PadB49)
- PCI4 pad B5: (no net) -> Net-(PCI4-PadB5)
- PCI4 pad B52: (no net) -> Net-(PCI4-PadB52)
- PCI4 pad B53: (no net) -> Net-(PCI4-PadB53)
- PCI4 pad B54: (no net) -> Net-(PCI4-PadB54)
- PCI4 pad B55: (no net) -> Net-(PCI4-PadB55)
- PCI4 pad B56: (no net) -> Net-(PCI4-PadB56)
- PCI4 pad B57: (no net) -> Net-(PCI4-PadB57)
- PCI4 pad B58: (no net) -> Net-(PCI4-PadB58)
- PCI4 pad B59: (no net) -> Net-(PCI4-PadB59)
- PCI4 pad B6: (no net) -> Net-(PCI4-PadB6)
- PCI4 pad B60: (no net) -> Net-(PCI4-PadB60)
- PCI4 pad B61: (no net) -> Net-(PCI4-PadB61)
- PCI4 pad B62: (no net) -> Net-(PCI4-PadB62)
- PCI4 pad B7: (no net) -> Net-(PCI4-PadB7)
- PCI4 pad B8: (no net) -> Net-(PCI4-PadB8)
- PCI4 pad B9: (no net) -> Net-(PCI4-PadB9)
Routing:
- net GND: track 547.4 -> 33.2 mm
- net Net-(CPU1-PadA19): track 115.7 -> 0.00 mm
- net Net-(CPU1-PadA11): track 104.0 -> 0.00 mm
- net PWR_+5V: track 93.2 -> 0.00 mm
- net (no net): track 90.2 -> 0.00 mm
- net PWR_-12V: track 59.4 -> 0.00 mm
- net PWR_-5V: track 54.9 -> 0.00 mm, vias 1 -> 0
- net PWR_+12V: track 22.3 -> 0.00 mm
- net PWR_+3.3V: track 9.70 -> 0.00 mm
- net Net-(CPU1-PadAN1): track 2.54 -> 0.00 mm
- net CPU_D9: vias 0 -> 1
- net CPU_D58: vias 0 -> 1
- net CPU_D57: vias 0 -> 1
- net CPU_D4: vias 0 -> 1
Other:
- copper layers 4 -> 6
